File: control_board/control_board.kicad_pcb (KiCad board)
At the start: 2 copper layers, 50.8 x 76.2 mm, 41 parts, among them J1 Conn_01x08_Male, K1 G5Q-1A, Q1 Q_NPN_BEC, U1 MC78M05_TO252, U2 TSR_1-24120, U3 74LS02, U4 74LS02, U5 Conn_01x08_Male

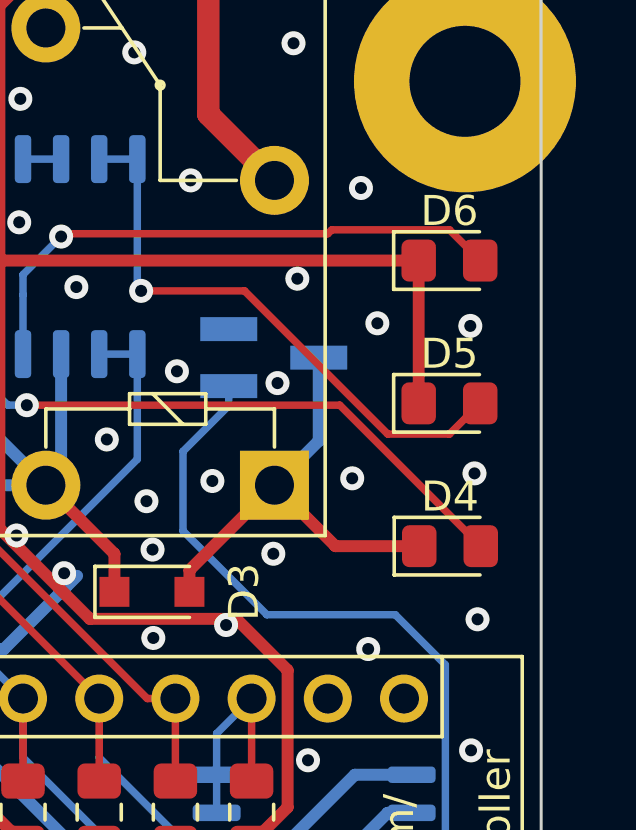
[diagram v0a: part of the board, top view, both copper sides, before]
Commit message: Change LED silkscreen
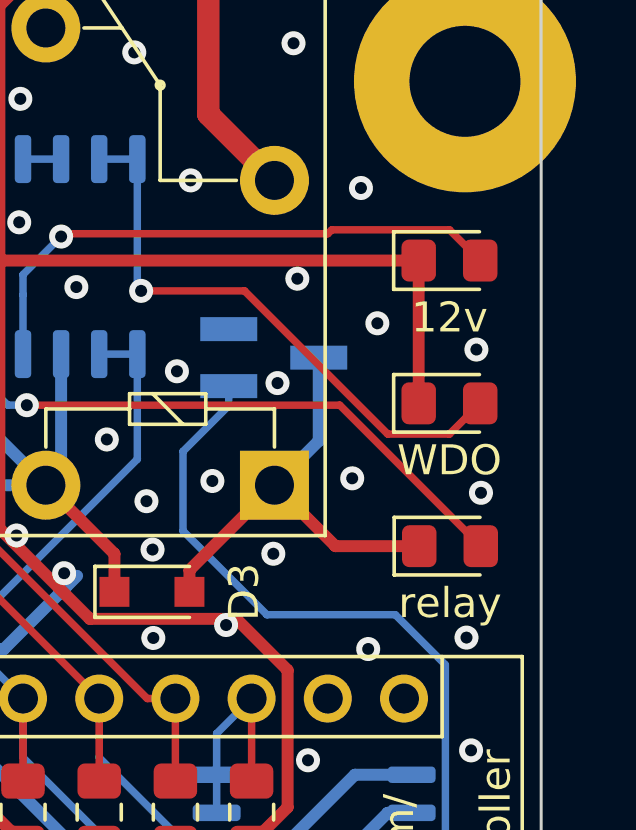
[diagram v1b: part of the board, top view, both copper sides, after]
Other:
- board text added: "12v"
- board text added: "WDO"
- board text added: "relay"

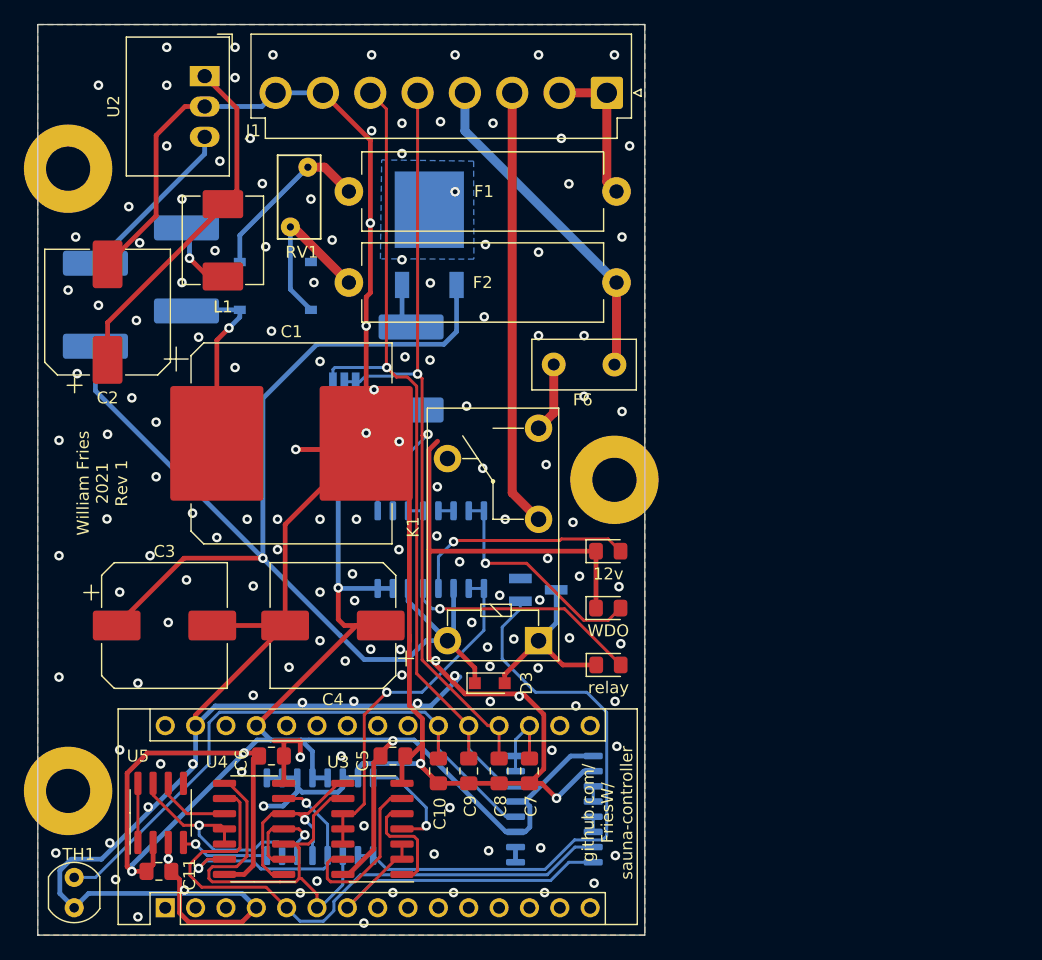
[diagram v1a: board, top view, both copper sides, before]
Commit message: Adjust mounting points
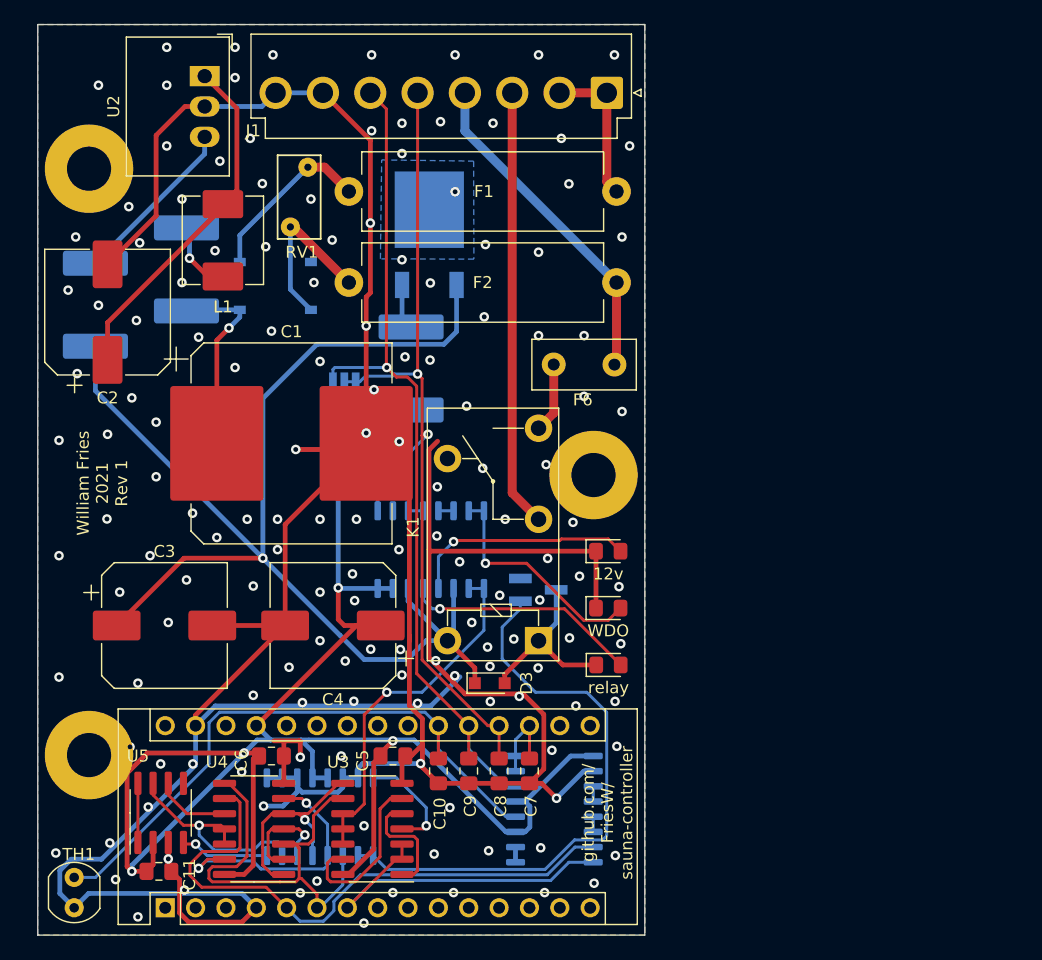
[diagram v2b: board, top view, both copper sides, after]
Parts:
- moved REF** 3.47 mm to (114.8, 85.3)
- moved REF** 1.80 mm to (157.0, 61.8)
- moved REF** 1.75 mm to (114.8, 36.2)
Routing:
- net GND: vias 151 -> 150
- net (no net): vias 0 -> 1
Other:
- board text removed: "JLCJLCJLCJLC"
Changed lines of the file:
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@@
   (general
     (thickness 1.6)
-    (drawings 18)
+    (drawings 17)
     (tracks 623)
     (zones 0)
@@
   )
   (module MountingHole:MountingHole_3.7mm_Pad (layer F.Cu)
-    (at 113.03 36.195)
+    (at 114.78 36.195)
     (descr "Mounting Hole 3.7mm")
     (tags "mounting hole 3.7mm")
@@
   )
   (module MountingHole:MountingHole_3.7mm_Pad (layer F.Cu)
-    (at 113.03 88.265)
+    (at 114.78 85.265)
     (descr "Mounting Hole 3.7mm")
     (tags "mounting hole 3.7mm")
@@
   )
   (module MountingHole:MountingHole_3.7mm_Pad (layer F.Cu)
-    (at 158.75 62.23)
+    (at 157 61.83)
     (descr "Mounting Hole 3.7mm")
     (tags "mounting hole 3.7mm")
@@
       (effects (font (size 1 1) (thickness 0.15)))
     )
+    (fp_text user %R (at 0.3 0) (layer F.Fab)
+      (effects (font (size 1 1) (thickness 0.15)))
+    )
+    (fp_circle (center 0 0) (end 3.7 0) (layer Cmts.User) (width 0.15))
     (fp_circle (center 0 0) (end 3.95 0) (layer F.CrtYd) (width 0.05))
-    (fp_circle (center 0 0) (end 3.7 0) (layer Cmts.User) (width 0.15))
-    (fp_text user %R (at 0.3 0) (layer F.Fab)
-      (effects (font (size 1 1) (thickness 0.15)))
-    )
     (pad 1 thru_hole circle (at 0 0) (size 7.4 7.4) (drill 3.7) (layers *.Cu *.Mask))
   )
@@
   )
   (gr_text https://github.com/FriesW/sauna-controller (at 149.479 51.3588 90) (layer B.SilkS)
-    (effects (font (size 1 1) (thickness 0.15)) (justify mirror))
-  )
-  (gr_text JLCJLCJLCJLC (at 122.0216 72.644) (layer B.SilkS)
     (effects (font (size 1 1) (thickness 0.15)) (justify mirror))
   )
@@
   (via (at 152.4 50.165) (size 0.8) (drill 0.4) (layers F.Cu B.Cu) (net 7))
   (via (at 156.21 55.245) (size 0.8) (drill 0.4) (layers F.Cu B.Cu) (net 7))
-  (via (at 159.385 56.515) (size 0.8) (drill 0.4) (layers F.Cu B.Cu) (net 7))
+  (via (at 159.385 56.515) (size 0.8) (drill 0.4) (layers F.Cu B.Cu) (net 0))
   (via (at 153.035 60.96) (size 0.8) (drill 0.4) (layers F.Cu B.Cu) (net 7))
   (via (at 140.97 32.385) (size 0.8) (drill 0.4) (layers F.Cu B.Cu) (net 7))
@@
   (via (at 119.888 68.58) (size 0.8) (drill 0.4) (layers F.Cu B.Cu) (net 7))
   (via (at 112.268 78.74) (size 0.8) (drill 0.4) (layers F.Cu B.Cu) (net 7))
-  (via (at 117.348 84.836) (size 0.8) (drill 0.4) (layers F.Cu B.Cu) (net 7))
   (via (at 118.872 79.248) (size 0.8) (drill 0.4) (layers F.Cu B.Cu) (net 7))
   (via (at 128.524 80.264) (size 0.8) (drill 0.4) (layers F.Cu B.Cu) (net 7))
@@
   (via (at 159.2834 75.946) (size 0.8) (drill 0.4) (layers F.Cu B.Cu) (net 7))
   (via (at 158.8008 80.772) (size 0.8) (drill 0.4) (layers F.Cu B.Cu) (net 7))
+  (via (at 118.2116 84.582) (size 0.8) (drill 0.4) (layers F.Cu B.Cu) (net 7))
   (segment (start 146.558 82.804) (end 146.558 85.555) (width 0.25) (layer F.Cu) (net 8))
   (segment (start 149.672 87.884) (end 150.472 87.884) (width 0.25) (layer B.Cu) (net 8))

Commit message: New mount hole spacing, new layout
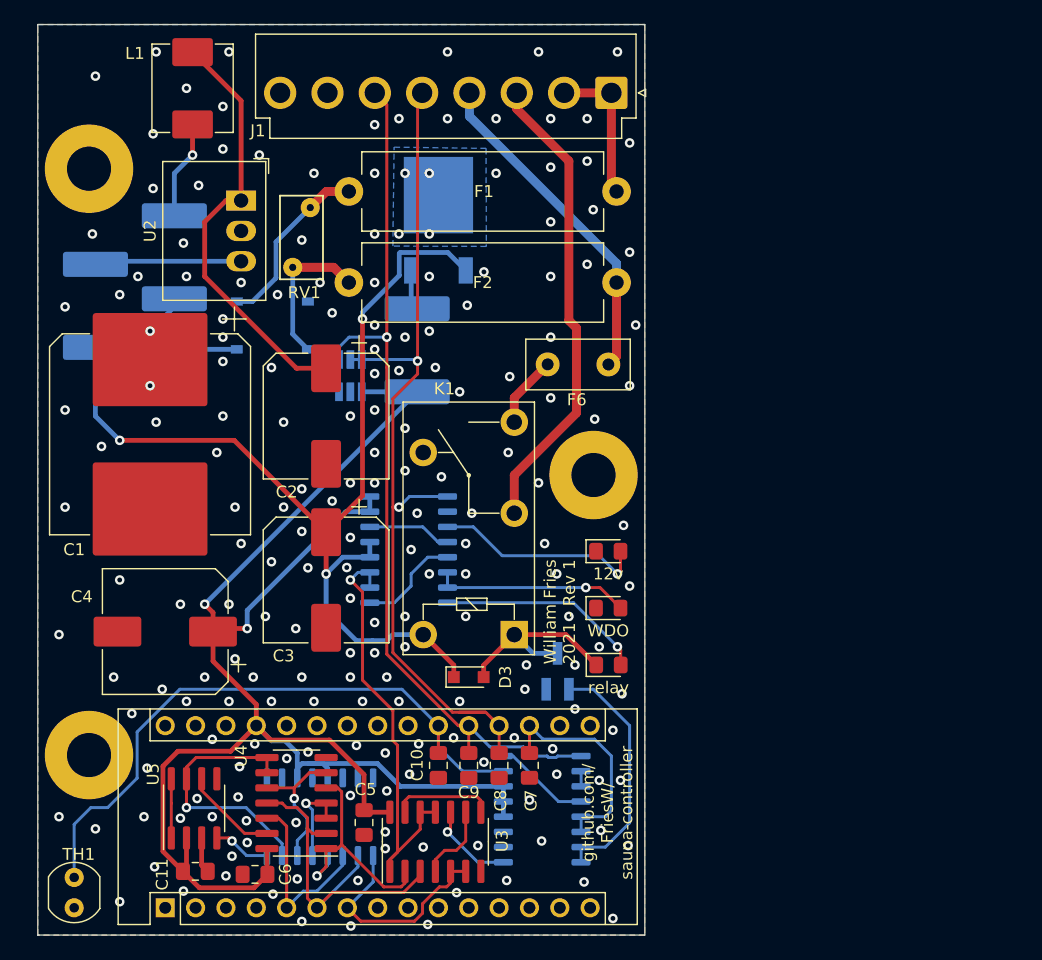
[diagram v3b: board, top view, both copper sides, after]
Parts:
- moved C2 20.3 mm to (134.6, 56.9), turned to 270 degrees
- moved C3 14.1 mm to (134.6, 70.6), turned to 270 degrees
- moved C4 14.0 mm to (121.2, 74.9)
- moved L1 13.0 mm to (123.4, 29.5)
- moved C1 11.9 mm to (119.9, 58.4), turned to 270 degrees
- moved U2 10.9 mm to (127.5, 38.9)
- moved C6 10.0 mm to (128.7, 95.2), turned to 180 degrees
- moved Q1 7.00 mm to (154.0, 78.3), turned to 90 degrees
- moved C5 6.07 mm to (137.8, 90.9), turned to 270 degrees
- moved U3 5.38 mm to (143.8, 92.5), turned to 90 degrees
- moved U4 4.16 mm to (132.1, 89.3)
- moved RV1 3.39 mm to (131.8, 44.5)
- moved D1 3.31 mm to (130.1, 49.3)
- moved C11 3.05 mm to (123.7, 95.0)
- moved U5 2.82 mm to (123.6, 89.7)
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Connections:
- RN1 pad 1: GND -> /p_cmd
- RN1 pad 10: GND -> Net-(RN1-Pad10)
- RN1 pad 11: Net-(RN1-Pad11) -> Net-(RN1-Pad10)
- RN1 pad 12: Net-(RN1-Pad11) -> Net-(RN1-Pad12)
- RN1 pad 13: Net-(RN1-Pad13) -> Net-(A1-Pad18)
- RN1 pad 14: Net-(RN1-Pad13) -> Net-(A1-Pad18)
- RN1 pad 15: /wd_kick -> Net-(Q1-Pad1)
- RN1 pad 16: /p_rqst -> Net-(Q1-Pad1)
- RN1 pad 3: +5V -> GND
- RN1 pad 4: Net-(A1-Pad21) -> +5V
- RN1 pad 6: /sensor_a -> +5V
- RN1 pad 7: Net-(A1-Pad18) -> Net-(A1-Pad21)
- RN1 pad 8: Net-(A1-Pad18) -> Net-(RN1-Pad12)
- RN1 pad 9: +5V -> /sensor_a
- RN2 pad 1: Net-(Q1-Pad1) -> /p_rqst
- RN2 pad 11: GND -> +5V
- RN2 pad 12: +5V -> GND
- RN2 pad 16: /p_cmd -> GND
- RN2 pad 2: Net-(Q1-Pad1) -> /sr_rst
- RN2 pad 3: /sr_rst -> /wd_kick
- RN3 pad 11: Net-(RN3-Pad11) -> Net-(D6-Pad2)
- RN3 pad 12: Net-(RN3-Pad11) -> Net-(RN3-Pad12)
- RN3 pad 13: Net-(RN3-Pad13) -> Net-(RN3-Pad1)
- RN3 pad 14: Net-(RN3-Pad13) -> Net-(D5-Pad2)
- RN3 pad 16: Net-(D5-Pad2) -> Net-(D4-Pad2)
- RN3 pad 2: Net-(RN3-Pad1) -> Net-(RN3-Pad2)
- RN3 pad 3: +12V -> Net-(RN3-Pad2)
- RN3 pad 4: Net-(D6-Pad2) -> +12V
- RN3 pad 5: Net-(D4-Pad2) -> +12V
- RN3 pad 6: +12V -> Net-(RN3-Pad12)
- U3 pad 1: Net-(U3-Pad1) -> Net-(RN3-Pad2)
- U3 pad 10: Net-(RN3-Pad1) -> /p_cmd
- U3 pad 11: Net-(RN3-Pad1) -> Net-(RN3-Pad2)
- U3 pad 12: Net-(RN3-Pad1) -> Net-(RN3-Pad2)
- U3 pad 2: /p_rqst -> Net-(RN2-Pad4)
- U3 pad 3: /p_rqst -> /sr_rst
- U3 pad 4: /p_cmd -> Net-(U3-Pad4)
- U3 pad 5: Net-(U3-Pad1) -> /p_rqst
- U3 pad 6: Net-(U3-Pad13) -> /p_rqst
- U3 pad 8: Net-(RN2-Pad5) -> Net-(U3-Pad13)
- U3 pad 9: /sr_rst -> Net-(U3-Pad4)
- U4 pad 1: Net-(RN2-Pad5) -> Net-(RN2-Pad4)
- U4 pad 10: Net-(U4-Pad10) -> Net-(RN2-Pad6)
- U4 pad 11: Net-(RN2-Pad7) -> /sr_rst
- U4 pad 12: Net-(RN2-Pad7) -> /wd_kick
- U4 pad 13: Net-(RN2-Pad4) -> Net-(U4-Pad13)
- U4 pad 2: Net-(RN2-Pad6) -> /sr_rst
- U4 pad 3: /sr_rst -> Net-(RN2-Pad5)
- U4 pad 4: Net-(RN2-Pad6) -> Net-(RN2-Pad5)
- U4 pad 5: Net-(RN2-Pad5) -> Net-(RN2-Pad4)
- U4 pad 6: Net-(RN2-Pad4) -> Net-(RN2-Pad6)
- U4 pad 8: /sr_rst -> Net-(RN2-Pad7)
- U4 pad 9: /wd_kick -> Net-(RN2-Pad7)
- U5 pad 6: Net-(U4-Pad10) -> Net-(U4-Pad13)
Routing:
- net GND: track 318.6 -> 3.88 mm, vias 150 -> 194
- net Net-(RN3-Pad2): track 0.00 -> 35.7 mm, vias 0 -> 1
- net /wd_kick: track 49.3 -> 15.7 mm
- net Net-(Q1-Pad1): track 48.8 -> 20.6 mm
- net +12V: track 108.8 -> 87.2 mm, vias 1 -> 3
- net Net-(RN3-Pad1): track 29.8 -> 8.82 mm, vias 1 -> 0
- net +5V: track 155.1 -> 139.5 mm, vias 4 -> 2
- net Net-(A1-Pad18): track 7.04 -> 18.8 mm
- net Net-(RN2-Pad5): track 19.0 -> 7.56 mm
- net /p_rqst: track 29.7 -> 18.4 mm
- net Net-(U3-Pad1): track 9.56 -> 0.00 mm
- net /sr_rst: track 39.5 -> 30.1 mm
- net Net-(RN1-Pad12): track 0.00 -> 8.08 mm
- net Net-(U4-Pad13): track 0.00 -> 7.93 mm
- net Net-(RN3-Pad12): track 0.00 -> 7.03 mm
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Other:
- board text added: "William Fries 2021 - Rev 1"
- board text removed: "William Fries 2021 Rev 1"

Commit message: Round PCB corners
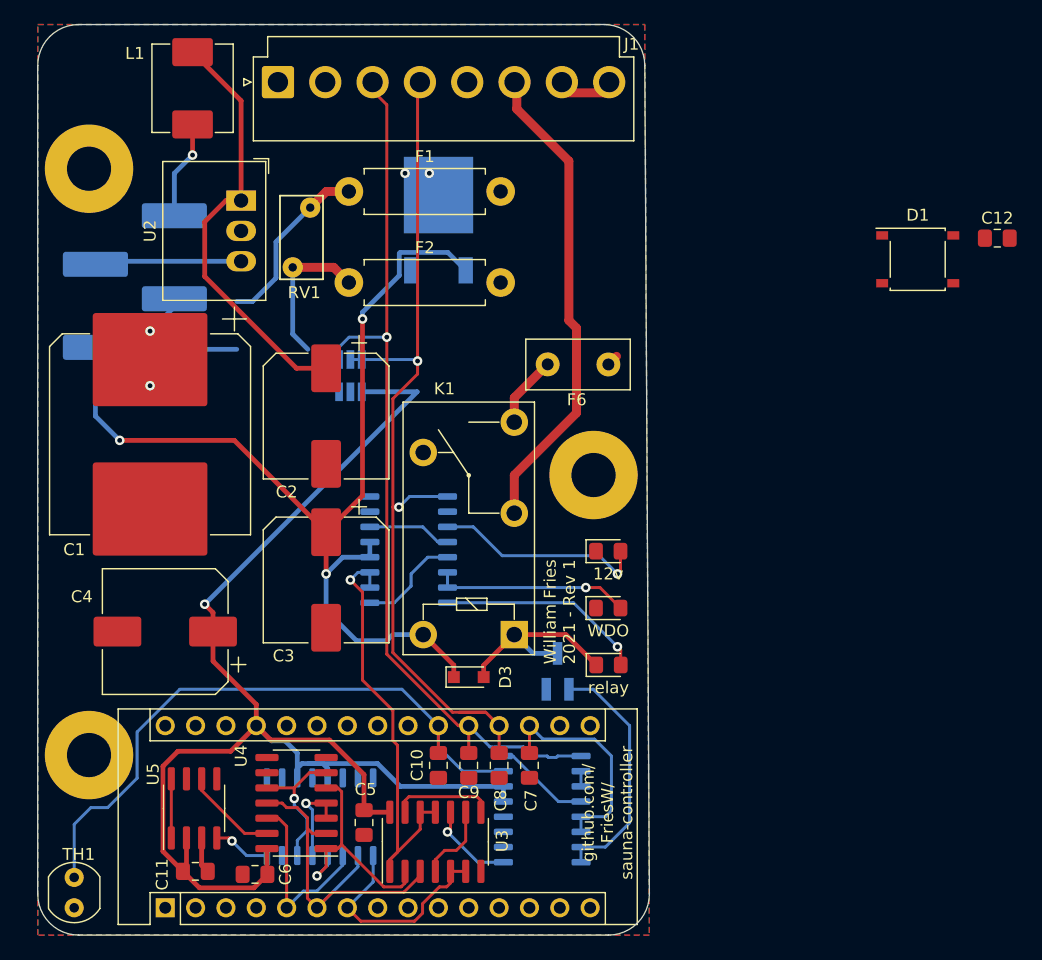
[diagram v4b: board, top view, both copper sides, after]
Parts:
- removed F5: Polyfuse, Fuse:Fuse_2920_7451Metric_Pad2.10x5.45mm_HandSolder
- added C12: 2.2u, Capacitor_SMD:C_0805_2012Metric_Pad1.18x1.45mm_HandSolder, F.Cu at (190.8, 42.0)
- D1: value D_Bridge_+A-A -> D_Bridge_+-AA; moved to F.Cu
- F1, F2: footprint Resistor_THT:R_Axial_Power_L20.0mm_W6.4mm_P22.40mm -> Resistor_THT:R_Axial_DIN0411_L9.9mm_D3.6mm_P12.70mm_Horizontal
- moved D1 54.3 mm to (184.1, 43.8)
- moved J1 27.9 mm to (130.6, 28.9), turned to 0 degrees
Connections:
- net Net-(A1-Pad11) renamed /aref_1k2
- A1 pad 10: Net-(A1-Pad10) -> /aref_1k1
- A1 pad 12: Net-(A1-Pad12) -> /aref_330
- A1 pad 8: Net-(A1-Pad8) -> /th1_tap
- A1 pad 9: Net-(A1-Pad9) -> /th2_tap
- D1 pad 2: /hv_03 -> GND
- D1 pad 3: GND -> /hv_02
- D1 pad 4: /hv_02 -> /hv_03
- J1 pad 1: GNDPWR -> GND
- J1 pad 2: GNDPWR -> GND
- J1 pad 3: /contactor_b -> /sensor_a
- J1 pad 4: AC -> /pot_a
- J1 pad 5: /pot_a -> AC
- J1 pad 6: /sensor_a -> /contactor_b
- J1 pad 7: GND -> GNDPWR
- J1 pad 8: GND -> GNDPWR
- RN1 pad 10: Net-(RN1-Pad10) -> /th1_tap
- RN1 pad 11: Net-(RN1-Pad10) -> /th1_tap
- RN1 pad 12: Net-(RN1-Pad12) -> /th2_tap
- RN1 pad 3: GND -> /raref_1k2
- RN1 pad 4: +5V -> /aref_1k1
- RN1 pad 8: Net-(RN1-Pad12) -> /th2_tap
- RN2 pad 10: GND -> +5V
- RN3 pad 10: Net-(RN3-Pad10) -> Net-(A1-Pad18)
- RN3 pad 7: +5V -> /aref_330
- U1 pad 3: /hc_03 -> +5V
- U4 pad 8: Net-(RN2-Pad7) -> Net-(C12-Pad1)
- U4 pad 9: Net-(RN2-Pad7) -> Net-(C12-Pad1)
- U5 pad 7: Net-(RN2-Pad7) -> Net-(C12-Pad1)
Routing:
- net AC: track 28.1 -> 0.97 mm
- net Net-(RN2-Pad7): track 22.0 -> 0.00 mm, vias 1 -> 0
- net +5V: track 139.5 -> 119.2 mm, vias 2 -> 1
- net GNDPWR: track 12.4 -> 3.96 mm
- net Net-(RN1-Pad12): track 8.08 -> 0.00 mm
- net /th2_tap: track 0.00 -> 8.08 mm
- net /hc_03: track 3.42 -> 0.00 mm
- net Net-(RN1-Pad10): track 1.27 -> 0.00 mm
- net /th1_tap: track 0.00 -> 1.27 mm
- net GND: vias 194 -> 2
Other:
- board size 50.8 x 76.2 mm -> 51.2 x 76.2 mm
